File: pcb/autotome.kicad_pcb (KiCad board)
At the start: 2 copper layers, 62 parts, among them SW1 SW_PUSH, SW10 SW_PUSH, SW11 SW_PUSH, SW12 SW_PUSH, SW13 SW_PUSH, SW14 SW_PUSH, SW15 SW_PUSH, SW16 SW_PUSH, SW17 SW_PUSH, SW18 SW_PUSH, SW19 SW_PUSH, SW2 SW_PUSH, SW20 SW_PUSH, SW21 SW_PUSH, SW22 SW_PUSH, SW23 SW_PUSH, SW24 SW_PUSH, SW25 RotaryEncoder_Switch, SW26 SW_PUSH, SW27 SW_PUSH, SW28 SW_PUSH, SW29 SW_PUSH, SW3 SW_PUSH, SW30 SW_PUSH, SW31 SW_SPDT, SW4 SW_PUSH, SW5 SW_PUSH, SW6 SW_PUSH, SW7 SW_PUSH, SW8 SW_PUSH, SW9 SW_PUSH, U1 ProMicro

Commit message: position keys
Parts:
- moved SW6 107.1 mm to (128.3, 35.7)
- moved BT1 106.9 mm to (239.4, 133.0)
- moved D1 106.9 mm to (237.6, 80.7)
- moved D10 106.9 mm to (237.6, 112.6)
- moved D11 106.9 mm to (248.3, 80.7)
- moved D12 106.9 mm to (248.3, 84.2)
- moved D13 106.9 mm to (248.3, 87.8)
- moved D14 106.9 mm to (248.3, 91.3)
- moved D15 106.9 mm to (248.3, 94.8)
- moved D16 106.9 mm to (248.3, 98.4)
- moved D17 106.9 mm to (248.3, 102.0)
- moved D18 106.9 mm to (248.3, 105.5)
- moved D19 106.9 mm to (248.3, 109.0)
- moved D2 106.9 mm to (237.6, 84.2)
- moved D20 106.9 mm to (248.3, 112.6)
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
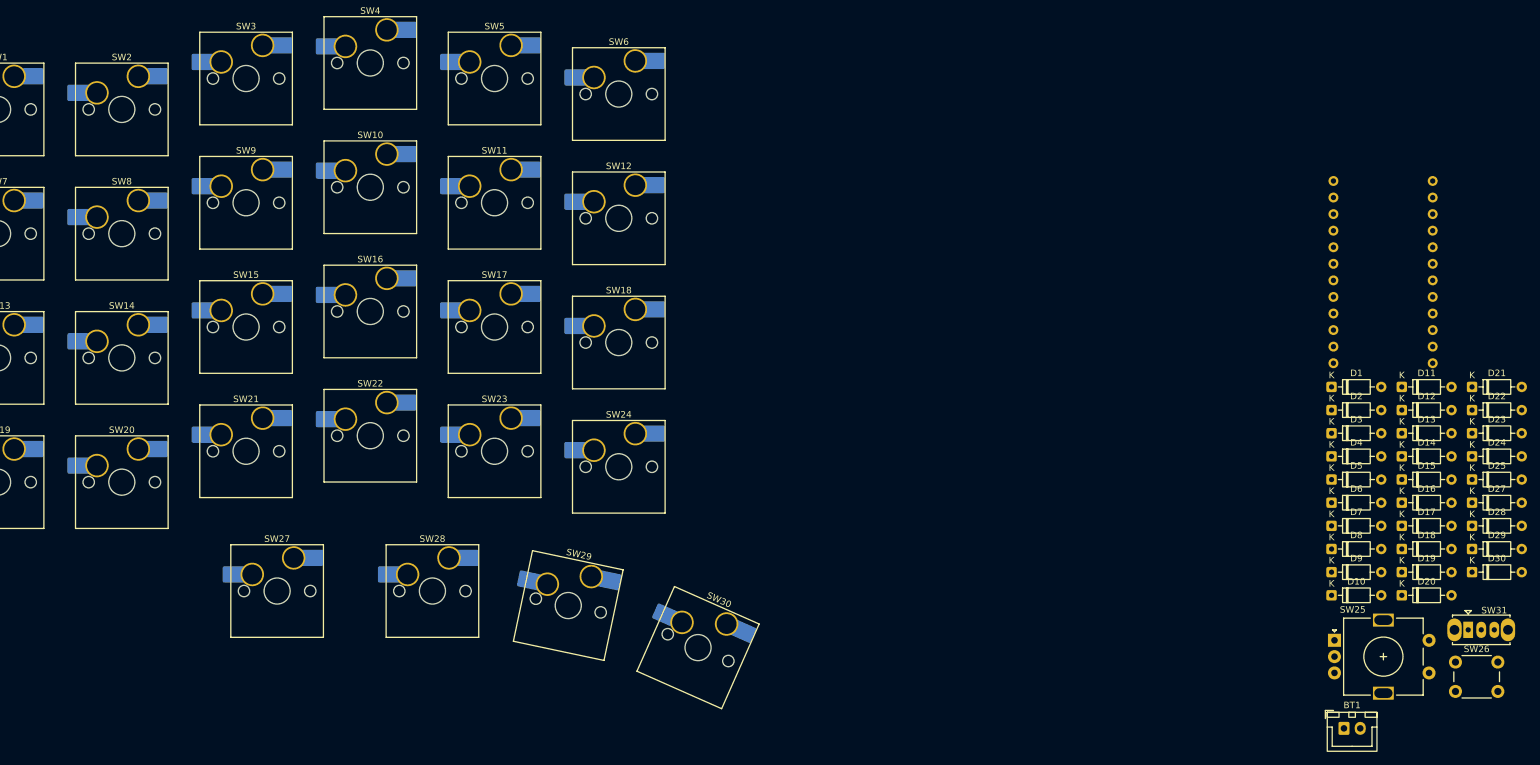
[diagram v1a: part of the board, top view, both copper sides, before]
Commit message: move diodes next to switches
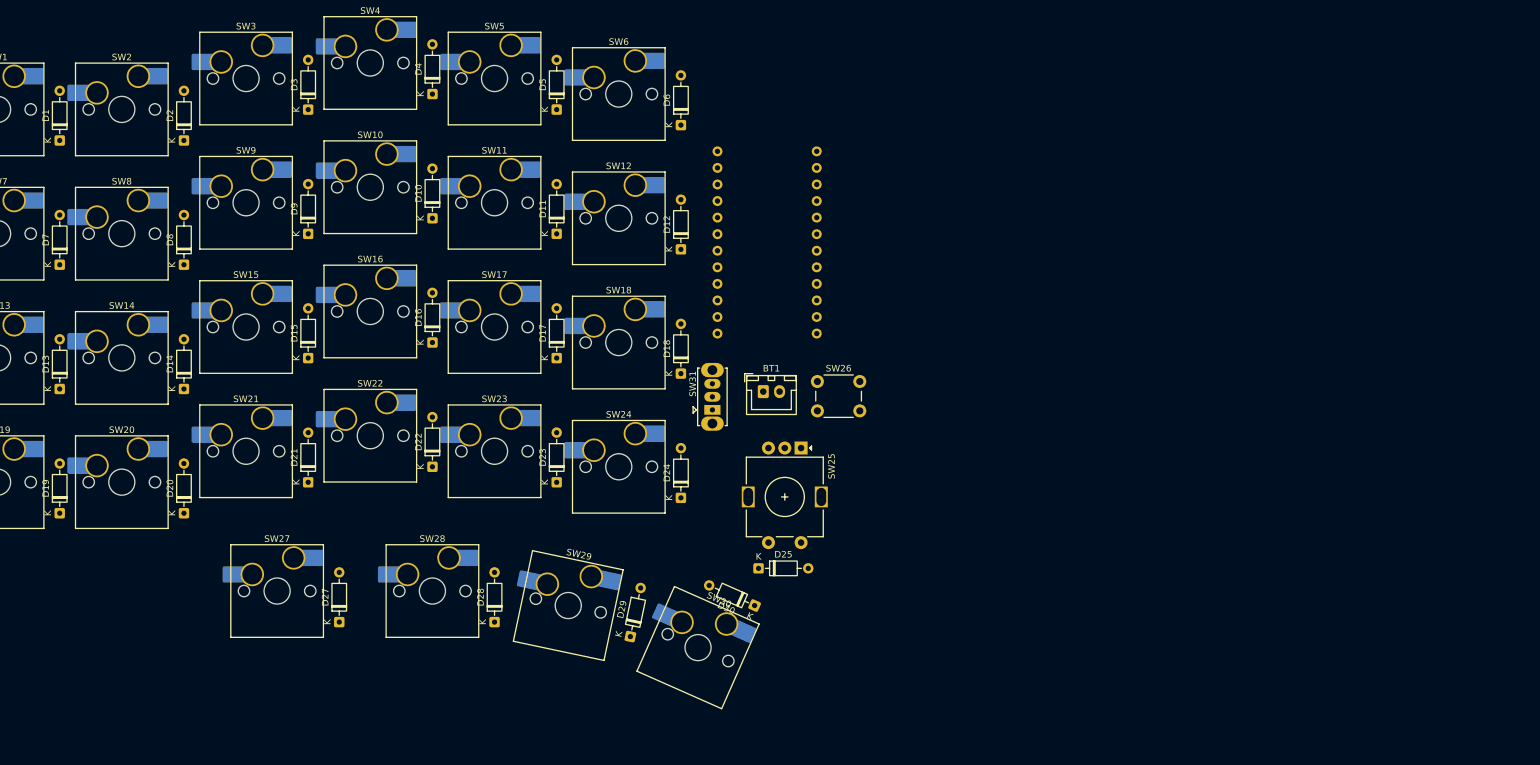
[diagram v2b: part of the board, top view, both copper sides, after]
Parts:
- moved D19 206.0 mm to (42.5, 100.0), turned to 90 degrees
- moved D13 205.9 mm to (42.5, 81.0), turned to 90 degrees
- moved D7 199.1 mm to (42.5, 61.9), turned to 90 degrees
- moved D1 198.6 mm to (42.5, 42.9), turned to 90 degrees
- moved D20 187.1 mm to (61.6, 100.0), turned to 90 degrees
- moved D14 187.0 mm to (61.6, 81.0), turned to 90 degrees
- moved D8 181.3 mm to (61.6, 61.9), turned to 90 degrees
- moved D2 180.7 mm to (61.6, 42.9), turned to 90 degrees
- moved D21 179.0 mm to (80.6, 95.3), turned to 90 degrees
- moved D27 174.6 mm to (85.4, 116.7), turned to 90 degrees
- moved D15 168.7 mm to (80.6, 76.2), turned to 90 degrees
- moved D9 165.3 mm to (80.6, 57.2), turned to 90 degrees
- moved D3 164.6 mm to (80.6, 38.1), turned to 90 degrees
- moved D22 159.6 mm to (99.7, 92.9), turned to 90 degrees
- moved D16 150.6 mm to (99.7, 73.8), turned to 90 degrees
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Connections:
- D25 pad 1: col 6 -> row 3
- SW25 pad S1: Net-(D25-A) -> col 6
- SW25 pad S2: row 3 -> Net-(D25-A)

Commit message: route temporarily
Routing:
- net col 0: track 0.00 -> 200.9 mm, vias 0 -> 10
- net col 1: track 0.00 -> 186.3 mm, vias 0 -> 8
- net col 2: track 0.00 -> 182.5 mm, vias 0 -> 6
- net col 3: track 0.00 -> 176.9 mm, vias 0 -> 4
- net row 3: track 0.00 -> 146.6 mm, vias 0 -> 2
- net col 4: track 0.00 -> 143.6 mm, vias 0 -> 2
- net col 5: track 0.00 -> 124.3 mm
- net row 0: track 0.00 -> 124.3 mm
- net row 4: track 0.00 -> 116.9 mm
- net row 2: track 0.00 -> 116.0 mm
- net row 1: track 0.00 -> 108.0 mm
- net B-: track 0.00 -> 59.9 mm
- net col 6: track 0.00 -> 48.0 mm
- net B+: track 0.00 -> 43.1 mm, vias 0 -> 2
- net RST: track 0.00 -> 37.5 mm
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
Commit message: reset pcb, place keys on a simple grid
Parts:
- removed SW26: SW_PUSH, Button_Switch_THT:SW_PUSH_6mm
- U1: moved to F.Cu
- moved D19 207.6 mm to (247.7, 132.1), turned to 0 degrees
- moved D13 207.3 mm to (247.7, 110.8), turned to 0 degrees
- moved D7 204.3 mm to (236.9, 125.0), turned to 0 degrees
- moved D1 203.6 mm to (236.9, 103.7), turned to 0 degrees
- moved D20 189.4 mm to (247.7, 135.6), turned to 0 degrees
- moved D14 189.0 mm to (247.7, 114.3), turned to 0 degrees
- moved D8 187.5 mm to (236.9, 128.5), turned to 0 degrees
- moved D2 186.7 mm to (236.9, 107.2), turned to 0 degrees
- moved D21 178.0 mm to (258.4, 103.7), turned to 0 degrees
- moved D9 173.3 mm to (236.9, 132.1), turned to 0 degrees
- moved D27 173.1 mm to (258.4, 121.4), turned to 0 degrees
- moved D3 172.3 mm to (236.9, 110.8), turned to 0 degrees
- moved D15 172.1 mm to (247.7, 117.8), turned to 0 degrees
- moved D22 159.4 mm to (258.4, 107.2), turned to 0 degrees
- moved D10 159.2 mm to (236.9, 135.6), turned to 0 degrees
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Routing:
- net col 0: track 200.9 -> 0.00 mm, vias 10 -> 0
- net col 1: track 186.3 -> 0.00 mm, vias 8 -> 0
- net col 2: track 182.5 -> 0.00 mm, vias 6 -> 0
- net col 3: track 176.9 -> 0.00 mm, vias 4 -> 0
- net row 3: track 146.6 -> 0.00 mm, vias 2 -> 0
- net col 4: track 143.6 -> 0.00 mm, vias 2 -> 0
- net col 5: track 124.3 -> 0.00 mm
- net row 0: track 124.3 -> 0.00 mm
- net row 4: track 116.9 -> 0.00 mm
- net row 2: track 116.0 -> 0.00 mm
- net row 1: track 108.0 -> 0.00 mm
- net B-: track 59.9 -> 0.00 mm
- net col 6: track 48.0 -> 0.00 mm
- net B+: track 43.1 -> 0.00 mm, vias 2 -> 0
- net RST: track 37.5 -> 0.00 mm
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
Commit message: place diodes
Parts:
- moved D19 210.6 mm to (37.8, 114.3), turned to 90 degrees
- moved D13 210.4 mm to (37.8, 95.2), turned to 90 degrees
- moved D7 205.0 mm to (37.8, 76.2), turned to 90 degrees
- moved D1 204.5 mm to (37.8, 57.1), turned to 90 degrees
- moved D20 192.0 mm to (56.8, 114.3), turned to 90 degrees
- moved D14 191.8 mm to (56.8, 95.2), turned to 90 degrees
- moved D8 187.5 mm to (56.8, 76.2), turned to 90 degrees
- moved D2 186.9 mm to (56.8, 57.1), turned to 90 degrees
- moved D21 182.8 mm to (75.9, 114.3), turned to 90 degrees
- moved D15 173.2 mm to (75.9, 95.2), turned to 90 degrees
- moved D9 170.4 mm to (75.9, 76.2), turned to 90 degrees
- moved D3 169.7 mm to (75.9, 57.1), turned to 90 degrees
- moved D22 163.6 mm to (94.9, 114.3), turned to 90 degrees
- moved D16 154.9 mm to (94.9, 95.2), turned to 90 degrees
- moved D10 153.9 mm to (94.9, 76.2), turned to 90 degrees
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
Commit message: place keys correctly
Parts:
- moved D25 62.6 mm to (238.1, 161.9)
- moved D27 33.1 mm to (81.0, 131.0)
- moved SW27 33.1 mm to (71.4, 126.1)
- moved D30 30.3 mm to (142.4, 143.0), turned to 66.12 degrees
- moved D28 28.7 mm to (104.5, 131.0)
- moved SW28 28.7 mm to (94.9, 126.1)
- moved D29 28.0 mm to (124.1, 135.0), turned to 78.06 degrees
- moved SW29 26.8 mm to (115.8, 128.3), turned to -11.94 degrees
- moved SW30 26.7 mm to (135.7, 134.7), turned to -23.88 degrees
- moved D10 7.14 mm to (94.9, 69.1)
- moved D16 7.14 mm to (94.9, 88.1)
- moved SW10 7.14 mm to (85.4, 64.3)
- moved SW4 7.14 mm to (85.4, 45.2)
- moved D4 7.14 mm to (94.9, 50.0)
- moved D22 7.14 mm to (94.9, 107.2)
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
